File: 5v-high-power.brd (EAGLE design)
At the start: 92.7 x 34.6 mm, 31 parts, among them IC1 LM2576, J1 Bypass, J2 En, J3 12v, J4 5V Out, J5 LEN EN, J6 POWERPOLE_POWER10AWG, J7 POWERPOLE_POWER10AWG, Q1 SI4532ADY

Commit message: changed to correct powerpole version added current rating onto docu layer
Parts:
- J6, J7: value POWERPOLE_POWER10AWG -> POWERPOLE_POWER25A; device powerpoles:POWERPOLE_PAIR_10AWG -> powerpoles:POWERPOLE_PAIR_25A
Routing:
- net N$1: track 31.8 -> 32.6 mm
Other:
- board text added: "2Amp"
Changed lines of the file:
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@@
 <text x="85.09" y="62.865" size="1.4224" layer="51">Version 0.2</text>
 <text x="88.265" y="33.02" size="1.4224" layer="51">PJB</text>
+<text x="25.4" y="35.306" size="1.778" layer="51" rot="R90">2Amp</text>
 </plain>
 <attributes>
@@
 <attribute name="VALUE" x="35.528" y="59.436" size="1.27" layer="27" ratio="10" rot="R180"/>
 </element>
-<element name="J6" library="powerpoles" package="POWERPOLE_PAIR_10AWG" value="POWERPOLE_POWER10AWG" x="106.045" y="60.96"/>
-<element name="J7" library="powerpoles" package="POWERPOLE_PAIR_10AWG" value="POWERPOLE_POWER10AWG" x="26.325" y="58.855" rot="R270"/>
+<element name="J6" library="powerpoles" package="POWERPOLE_PAIR_25A" value="POWERPOLE_POWER25A" x="106.045" y="60.96"/>
+<element name="J7" library="powerpoles" package="POWERPOLE_PAIR_25A" value="POWERPOLE_POWER25A" x="26.325" y="58.855" rot="R270"/>
 </elements>
 <signals>
@@
 <wire x1="88.265" y1="60.96" x2="82.51" y2="60.96" width="1.016" layer="1"/>
 <contactref element="J6" pad="RED"/>
-<wire x1="82.51" y1="60.96" x2="102.145" y2="60.96" width="1.016" layer="16"/>
-<wire x1="102.145" y1="60.96" x2="106.426" y2="60.96" width="1.016" layer="16"/>
-<wire x1="106.426" y1="60.96" x2="106.426" y2="53.975" width="1.016" layer="16"/>
+<wire x1="82.51" y1="60.96" x2="102.108" y2="60.96" width="1.016" layer="16"/>
+<wire x1="102.108" y1="60.96" x2="102.108" y2="60.11" width="1.016" layer="16"/>
+<wire x1="102.108" y1="60.11" x2="102.095" y2="60.11" width="1.016" layer="16"/>
+<wire x1="102.095" y1="60.11" x2="106.426" y2="60.198" width="1.016" layer="16"/>
+<wire x1="106.426" y1="60.198" x2="106.426" y2="53.975" width="1.016" layer="16"/>
 <wire x1="106.426" y1="53.975" x2="109.22" y2="53.975" width="1.016" layer="16"/>
 <wire x1="109.22" y1="53.975" x2="109.22" y2="37.973" width="1.016" layer="16"/>
@@
 <wire x1="33.274" y1="61.595" x2="35.274" y2="61.595" width="1.016" layer="1"/>
 <contactref element="J7" pad="RED"/>
-<wire x1="26.325" y1="62.755" x2="26.325" y2="61.468" width="1.016" layer="1"/>
-<wire x1="26.325" y1="61.468" x2="33.274" y2="61.468" width="1.016" layer="1"/>
+<wire x1="25.475" y1="62.805" x2="25.563" y2="61.468" width="1.016" layer="1"/>
+<wire x1="25.563" y1="61.468" x2="33.274" y2="61.468" width="1.016" layer="1"/>
 </signal>
 </signals>

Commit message: Added additional USB footprints and rotated some powerpoles
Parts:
- removed X1: (no value), con-berg:PN87520
- added SJ1, SJ2, SJ3: (no value), jumper:SJ
- added U$2: USB_DUAL_VERT+HORIZTRIPPLE, power:USB_DUAL_HORIZ+VERT
- moved R2 2.54 mm to (94.6, 35.6)
- moved C3 2.29 mm to (89.2, 43.2)
- moved LED2 1.27 mm to (83.2, 35.6)
- moved J6 0.25 mm to (106.3, 61.0), turned to 180 degrees
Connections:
- new net N$3: SJ1.2, U$2.P2.3
- new net N$4: SJ1.1, U$2.P2.2
- new net N$5: SJ2.2, U$2.P3.3
- new net N$6: SJ2.1, U$2.P3.2
- new net N$7: SJ3.2, U$2.P1.3
- new net N$8: SJ3.1, U$2.P1.2
- net 5V: now also U$2.P1.1, U$2.P2.1, U$2.P3.1; no longer X1.1
- net GND: now also U$2.P1.4, U$2.P2.4, U$2.P3.4; no longer X1.4
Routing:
- net 5V: track 79.9 -> 87.1 mm
- net N$4: track 0.00 -> 2.64 mm
- net N$6: track 0.00 -> 2.62 mm
- net N$5: track 0.00 -> 2.62 mm
- net N$8: track 0.00 -> 2.52 mm
- net N$7: track 0.00 -> 2.52 mm
- net N$3: track 0.00 -> 2.17 mm
- net N$47: track 12.9 -> 11.6 mm
- net LEDGND: track 53.9 -> 52.6 mm

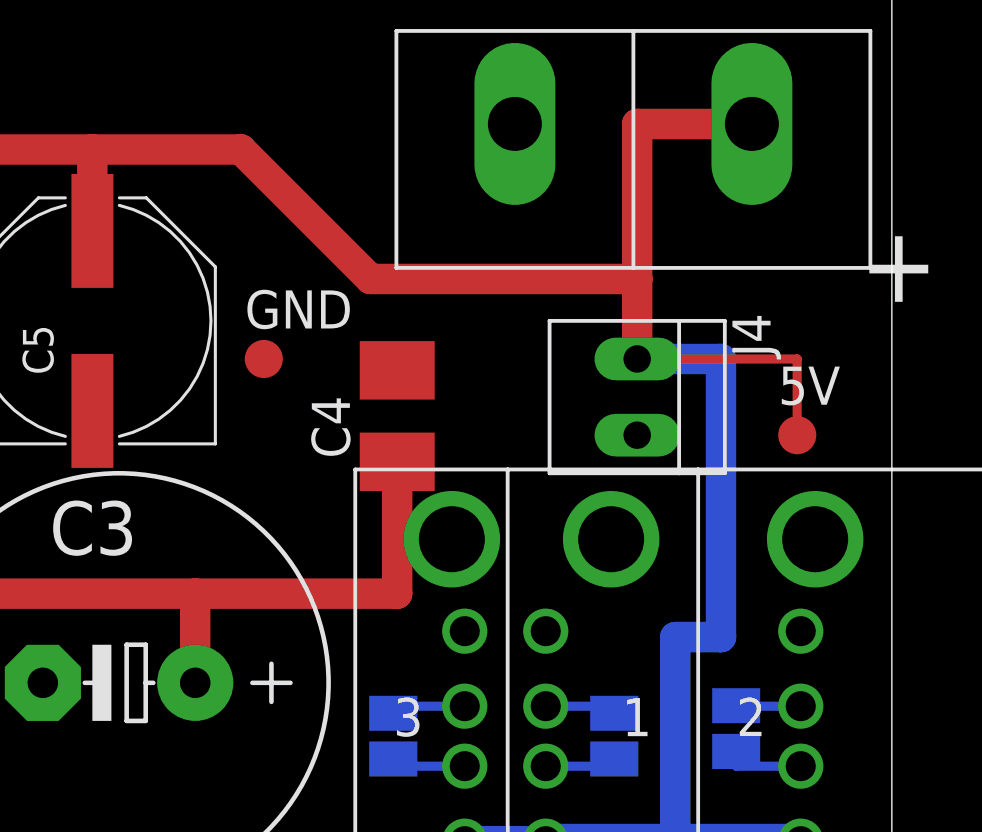
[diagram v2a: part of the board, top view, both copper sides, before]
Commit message: moved a couple of components
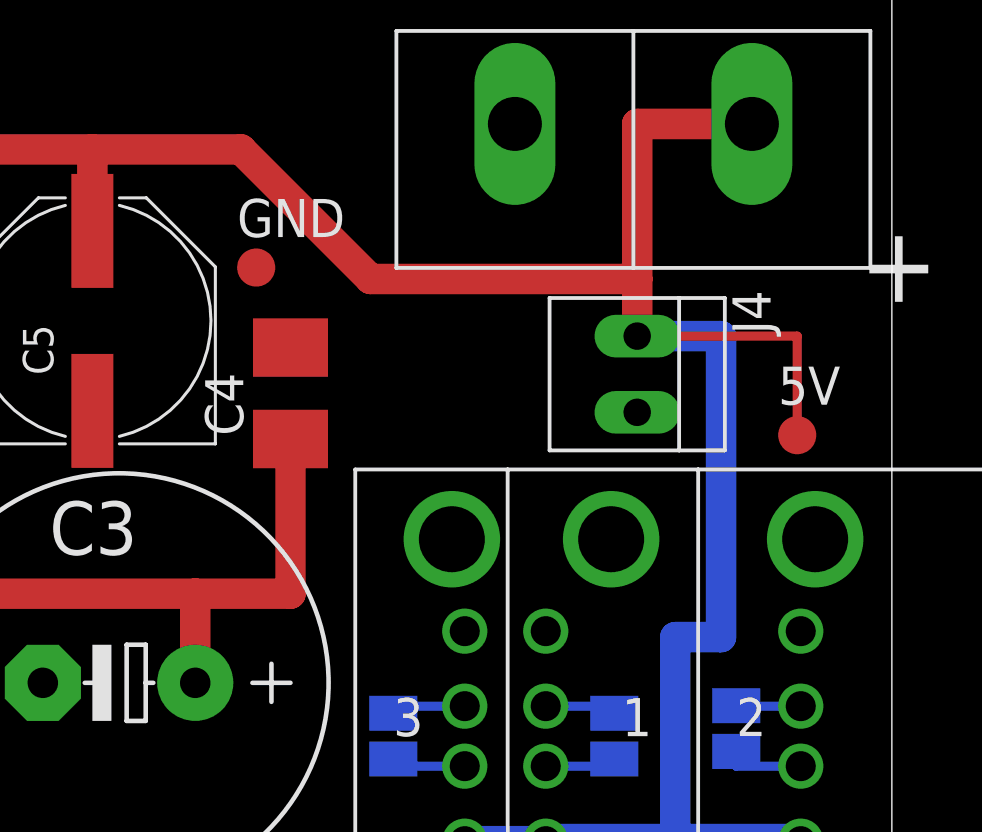
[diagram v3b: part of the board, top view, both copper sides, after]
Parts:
- moved C4 3.64 mm to (94.9, 52.8)
- moved GND 3.06 mm to (93.7, 57.0)
- moved J4 0.76 mm to (106.0, 53.5)
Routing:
- net N$103: track 54.3 -> 51.5 mm
- net 5V: track 87.1 -> 87.9 mm
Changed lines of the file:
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@@
 <attribute name="VALUE" x="93.091" y="40.767" size="1.778" layer="27" ratio="10" rot="R180"/>
 </element>
-<element name="C4" library="rcl" package="B/3528-21R" value="220uF Tant" x="98.425" y="52.07" smashed="yes" rot="R270">
-<attribute name="NAME" x="95.58" y="52.75" size="1.27" layer="25" rot="R270"/>
-<attribute name="VALUE" x="99.945" y="55.29" size="1.27" layer="27" rot="R270"/>
+<element name="C4" library="rcl" package="B/3528-21R" value="220uF Tant" x="94.869" y="52.832" smashed="yes" rot="R270">
+<attribute name="NAME" x="92.024" y="53.512" size="1.27" layer="25" rot="R270"/>
+<attribute name="VALUE" x="96.389" y="56.052" size="1.27" layer="27" rot="R270"/>
 </element>
 <element name="U$1" library="farnell-parts" package="DO-201AD" value="SF37" x="72.39" y="48.26" rot="MR90"/>
@@
 <attribute name="VALUE" x="46.228" y="35.306" size="1.27" layer="27" ratio="10" rot="R180"/>
 </element>
-<element name="J4" library="farnell-parts" package="2-MOLEX" value="5V Out" x="106.045" y="52.705" rot="R90"/>
+<element name="J4" library="farnell-parts" package="2-MOLEX" value="5V Out" x="106.045" y="53.467" rot="R90"/>
 <element name="LED1" library="led" package="CHIP-LED0805" value="12V" x="38.1" y="36.195" smashed="yes" rot="R180">
 <attribute name="VALUE" x="36.195" y="33.02" size="1.27" layer="27"/>
@@
 </element>
 <element name="D1" library="diode" package="SMB" value="" x="33.02" y="38.1" rot="R90"/>
-<element name="GND" library="testpad" package="B1,27" value="5V B" x="93.98" y="53.975">
-<attribute name="TP_SIGNAL_NAME" value="" x="93.98" y="53.975" size="1.778" layer="27" display="off"/>
+<element name="GND" library="testpad" package="B1,27" value="5V B" x="93.726" y="57.023">
+<attribute name="TP_SIGNAL_NAME" value="" x="93.726" y="57.023" size="1.778" layer="27" display="off"/>
 </element>
 <element name="J3" library="farnell-parts" package="2-MOLEX" value="12v" x="35.655" y="62.865" smashed="yes" rot="R270">
@@
 <wire x1="88.265" y1="60.96" x2="82.51" y2="60.96" width="1.016" layer="1"/>
 <contactref element="J6" pad="RED"/>
-<wire x1="106.426" y1="53.975" x2="109.22" y2="53.975" width="1.016" layer="16"/>
-<wire x1="109.22" y1="53.975" x2="109.22" y2="44.704" width="1.016" layer="16"/>
+<wire x1="106.426" y1="54.737" x2="109.22" y2="54.737" width="1.016" layer="16"/>
+<wire x1="109.22" y1="54.737" x2="109.22" y2="44.704" width="1.016" layer="16"/>
 <wire x1="109.22" y1="44.704" x2="107.696" y2="44.704" width="1.016" layer="16"/>
 <wire x1="107.696" y1="44.704" x2="107.696" y2="37.973" width="1.016" layer="16"/>
 <wire x1="107.696" y1="37.973" x2="103.335" y2="37.973" width="1.016" layer="16"/>
-<wire x1="111.76" y1="51.435" x2="111.76" y2="53.975" width="0.3048" layer="1"/>
-<wire x1="111.76" y1="53.975" x2="106.426" y2="53.975" width="0.3048" layer="1"/>
+<wire x1="111.76" y1="51.435" x2="111.76" y2="54.737" width="0.3048" layer="1"/>
+<wire x1="111.76" y1="54.737" x2="106.426" y2="54.737" width="0.3048" layer="1"/>
 <wire x1="110.249" y1="61.81" x2="106.426" y2="61.81" width="1.016" layer="1"/>
 <wire x1="106.426" y1="61.81" x2="106.426" y2="56.642" width="1.016" layer="1"/>
-<wire x1="106.426" y1="56.642" x2="106.426" y2="53.975" width="1.016" layer="1"/>
+<wire x1="106.426" y1="56.642" x2="106.426" y2="54.737" width="1.016" layer="1"/>
 <wire x1="88.265" y1="60.96" x2="93.218" y2="60.96" width="1.016" layer="1"/>
 <wire x1="93.218" y1="60.96" x2="97.536" y2="56.642" width="1.016" layer="1"/>
@@
 <wire x1="77.51" y1="60.96" x2="77.51" y2="59.69" width="1.016" layer="1"/>
 <wire x1="77.51" y1="59.69" x2="69.97" y2="59.69" width="1.016" layer="1"/>
-<wire x1="91.694" y1="46.1518" x2="98.425" y2="46.1518" width="1.016" layer="1"/>
-<wire x1="98.425" y1="46.1518" x2="98.425" y2="50.545" width="1.016" layer="1"/>
+<wire x1="91.694" y1="46.1518" x2="94.869" y2="46.1518" width="1.016" layer="1"/>
+<wire x1="94.869" y1="46.1518" x2="94.869" y2="51.307" width="1.016" layer="1"/>
 </signal>
 <signal name="N$104">
